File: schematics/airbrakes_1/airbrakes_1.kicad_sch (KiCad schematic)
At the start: 13 parts, among them U6 XL1509-3.3

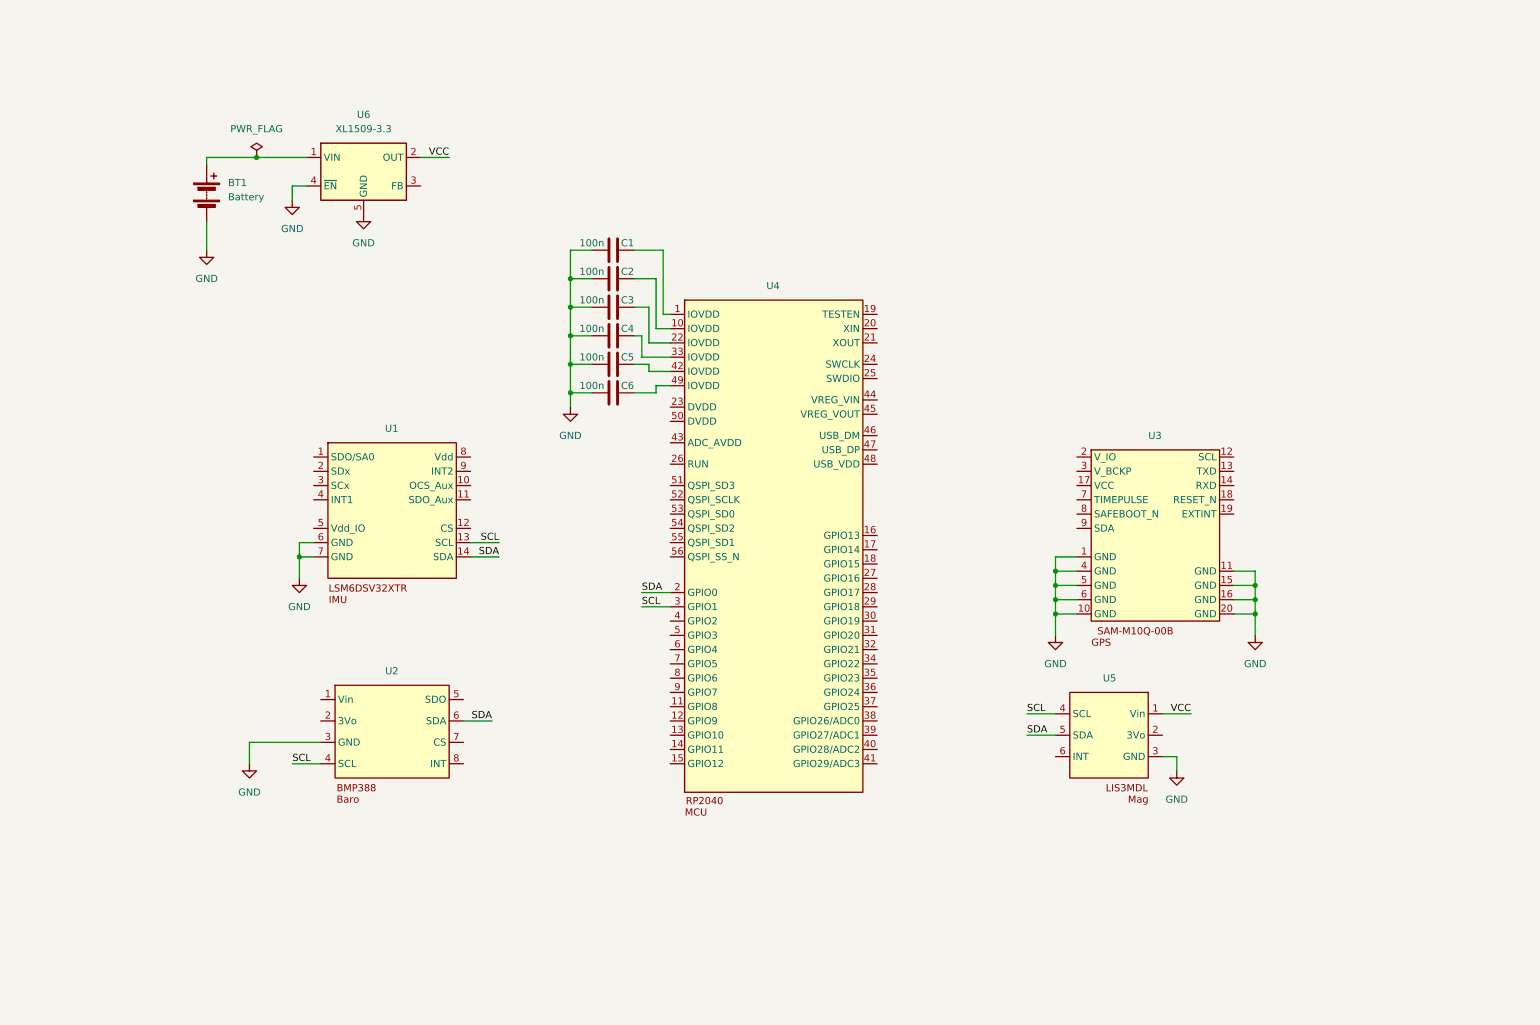
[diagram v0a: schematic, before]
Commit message: Route SPI/I2C connections to Baro, Mag, GPS; some other connections & notes
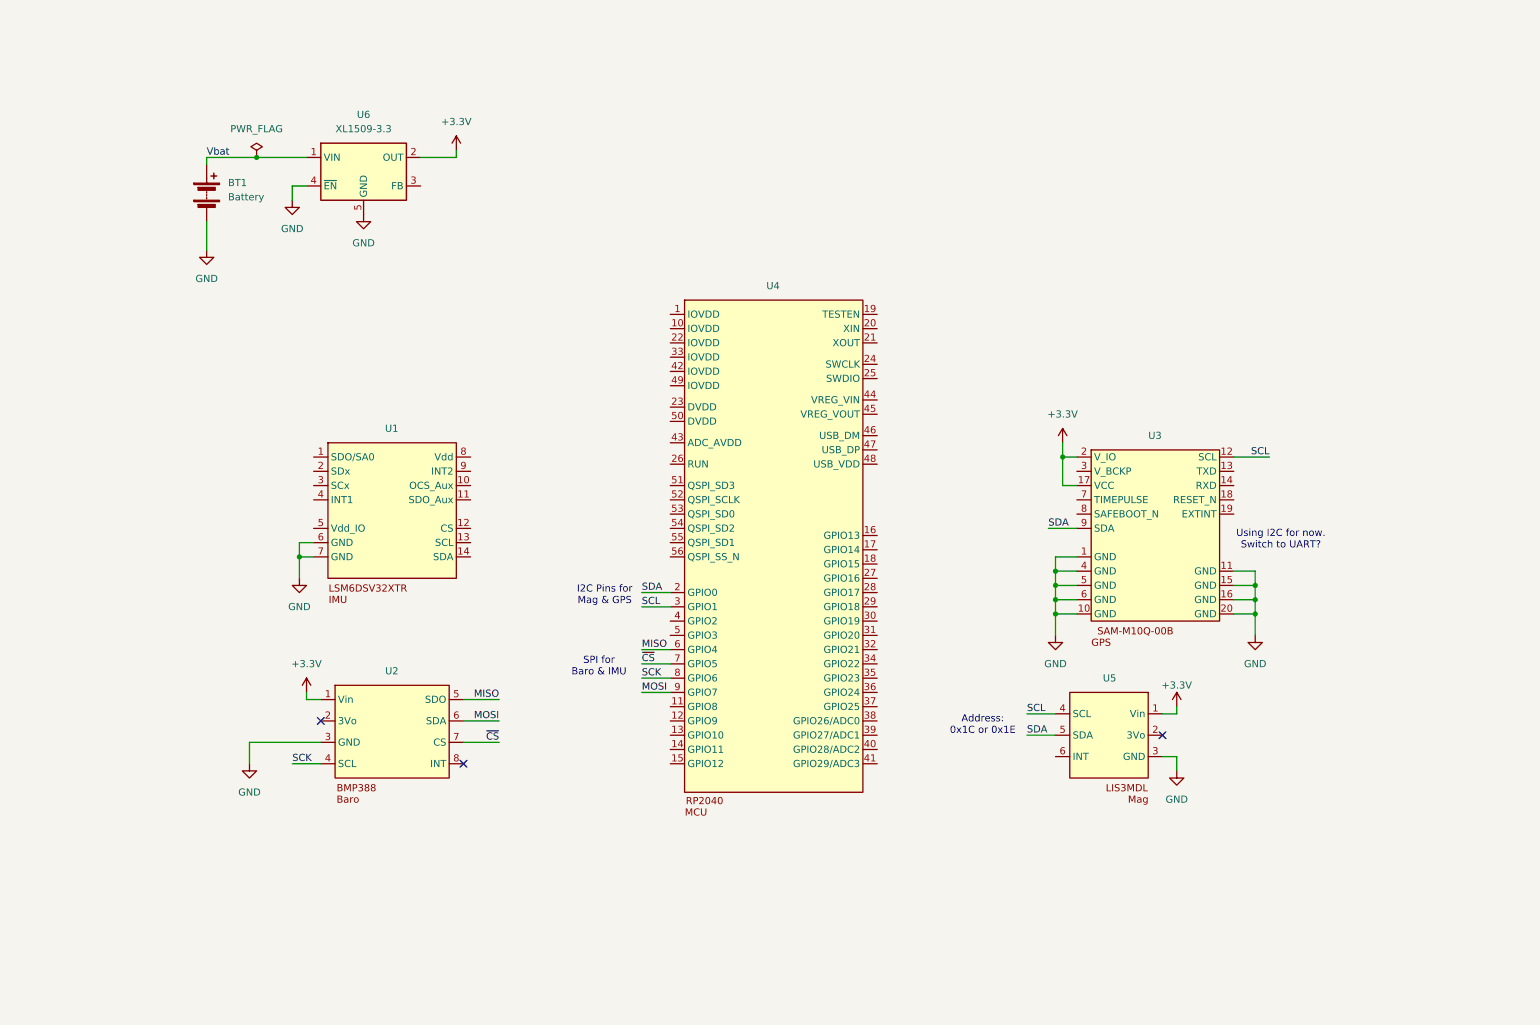
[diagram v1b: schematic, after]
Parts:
- removed C1, C2, C3, C4, C5, C6: 100n, symbol Device:C
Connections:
- net VCC is gone; now on net +3.3V: U5.1 (Vin), U6.2 (OUT)
- net SCL: now also U3.12 (SCL); no longer U1.13 (SCL), U2.4 (SCL)
- net SDA: now also U3.9 (SDA); no longer U1.14 (SDA), U2.6 (SDA)
- net +3.3V: now reaches U3.17 (VCC)
- net +3.3V: now also U2.1 (Vin), U3.2 (V_IO)
- net Vbat: now reaches BT1.1 (+), U6.1 (VIN)
- net MISO: now reaches U2.5 (SDO)
- net MISO: now also U4.6 (GPIO4)
- net ~{CS}: now reaches U2.7 (CS)
- net ~{CS}: now also U4.7 (GPIO5)
- net SCK: now reaches U4.8 (GPIO6)
- net SCK: now also U2.4 (SCL)
- net MOSI: now reaches U4.9 (GPIO7)
- net MOSI: now also U2.6 (SDA)
- no-connect marks 0 -> 3
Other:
- note added: "Address: 0x1C or 0x1E"
- note added: "I2C Pins for Mag & GPS"
- note added: "SPI for Baro & IMU"
- note added: "Using I2C for now. Switch to UART?"

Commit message: Finish communication routing, organize into sections
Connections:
- net +3.3V: now also U1.5 (Vdd_IO), U1.8 (Vdd)
- net GND: now also U1.2 (SDx), U1.3 (SCx)
- net MISO: now also U1.1 (SDO/SA0)
- net MOSI: now also U1.14 (SDA)
- net SCK: now also U1.13 (SCL)
- net ~{CS_imu}: now reaches U1.12 (CS)
- net ~{CS_imu}: now also U4.12 (GPIO9)
- net ~{CS} renamed ~{CS_baro}
- no-connect marks 3 -> 26
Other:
- note added: "Consider building out details, might use a premade board though"
- note added: "MCU"
- note added: "Power"
- note added: "Sensors"
- moved on the sheet: BT1, U1, U2, U3, U4, U5, U6

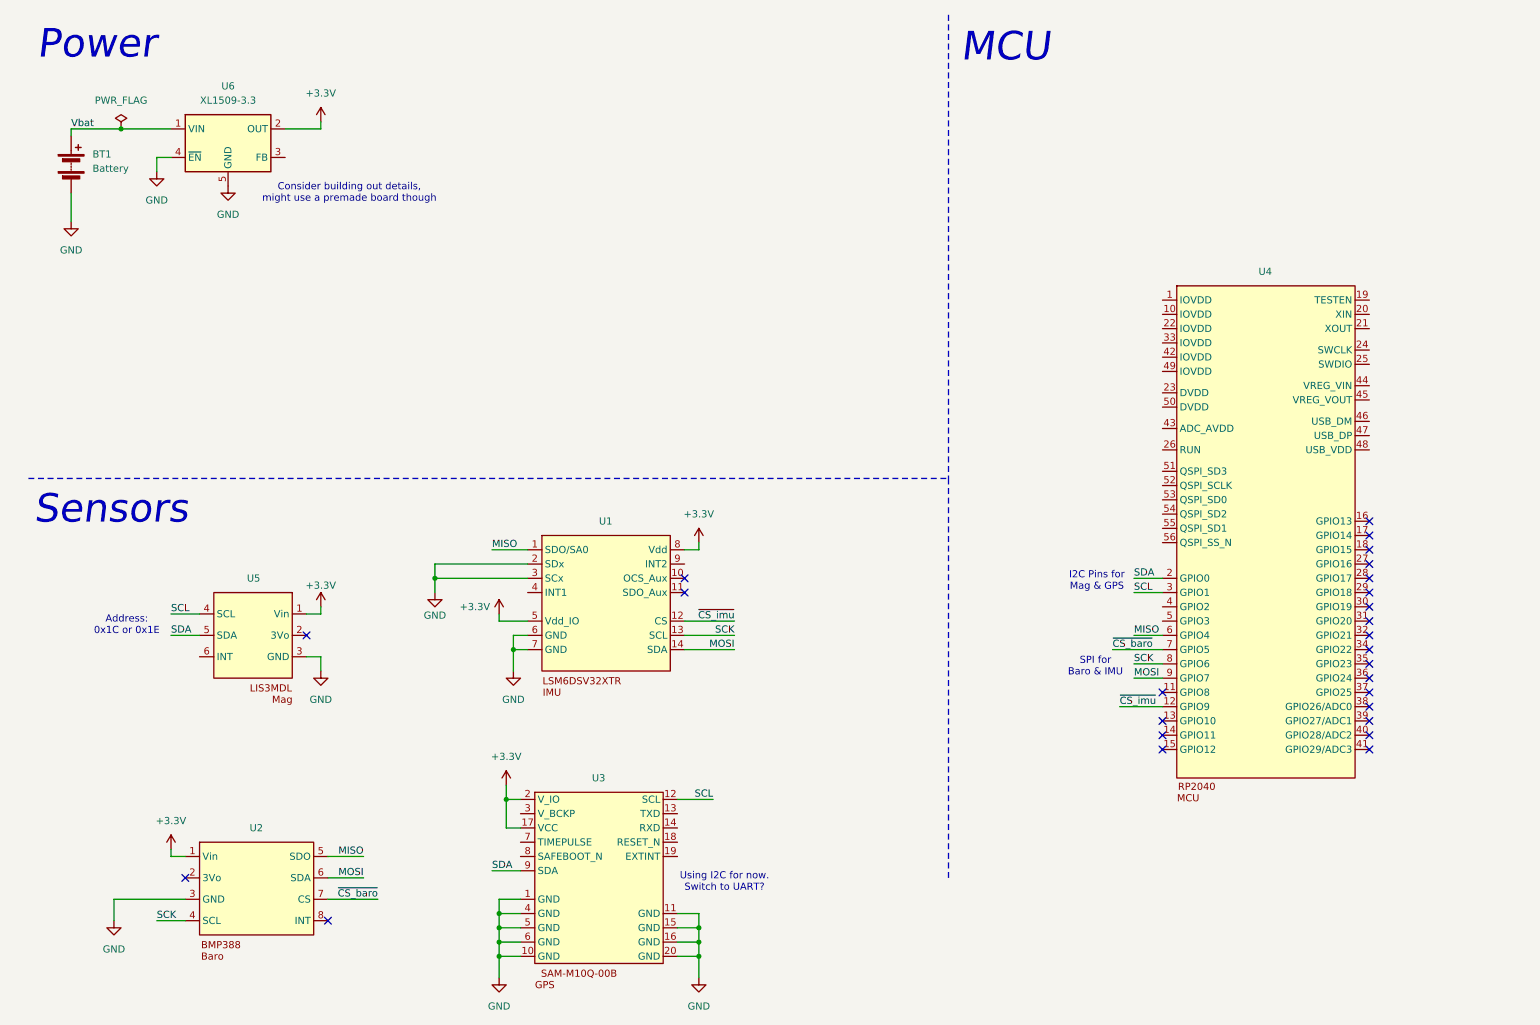
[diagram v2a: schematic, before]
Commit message: Add am-3637b motor
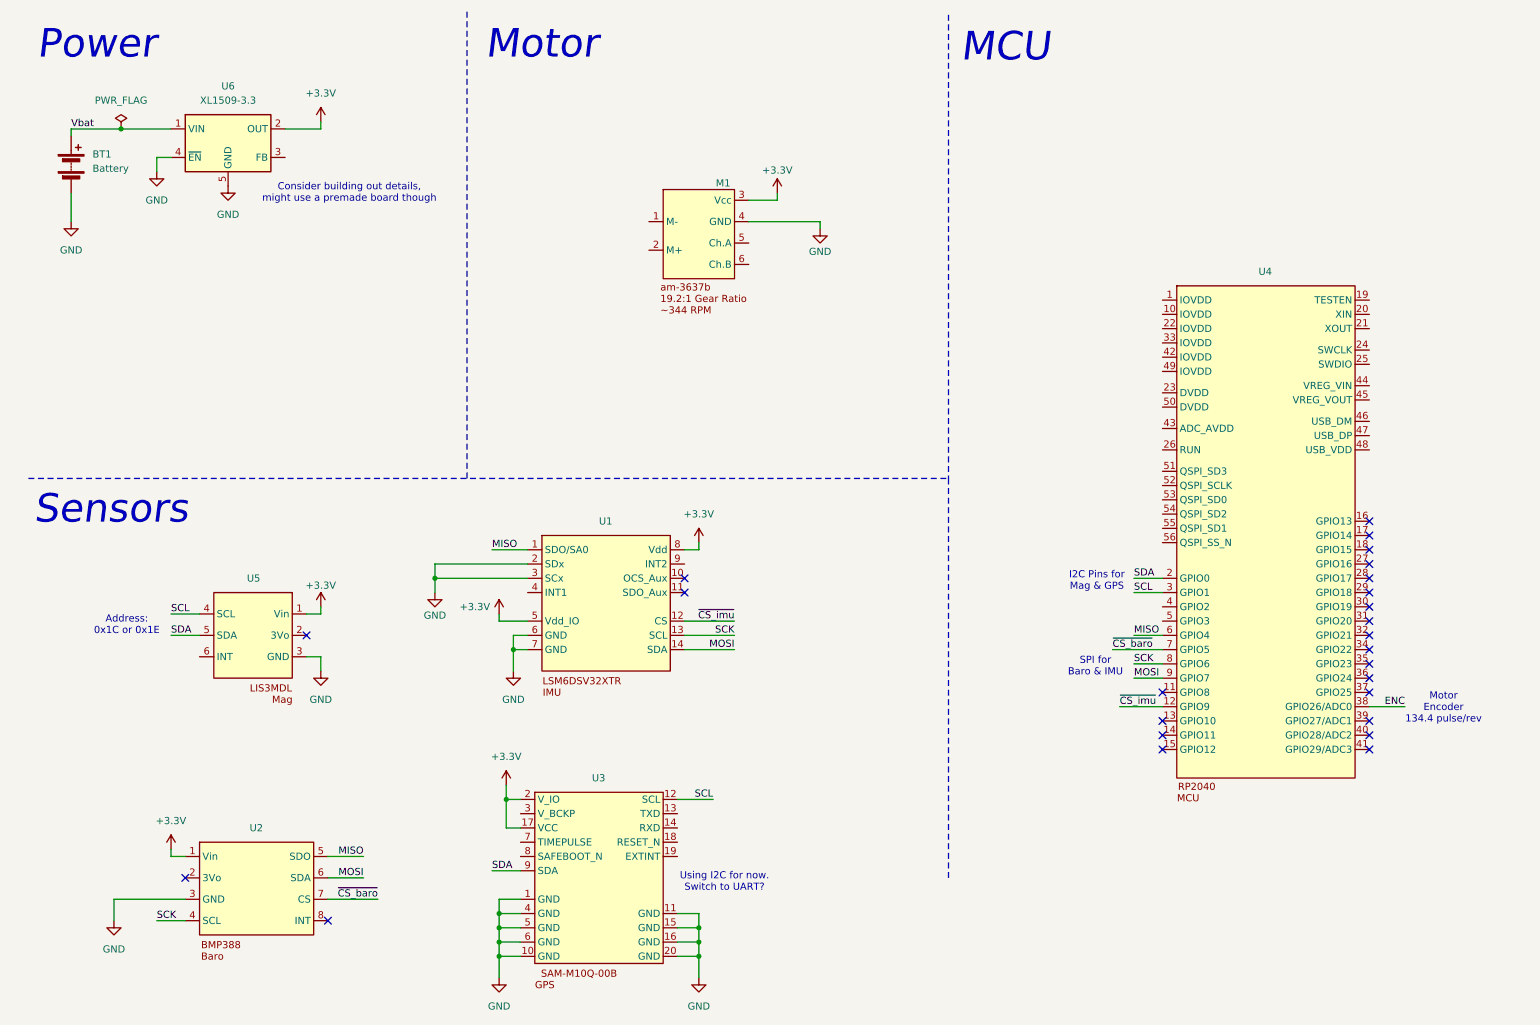
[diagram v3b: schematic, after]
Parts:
- added M1: (no value), symbol airbrakes_1:am-3637b
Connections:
- net +3.3V: now also M1.3 (Vcc)
- net GND: now also M1.4 (GND)
- net ENC: now reaches U4.38 (GPIO26/ADC0)
- no-connect marks 26 -> 25
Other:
- note added: "Motor"
- note added: "Motor Encoder 134.4 pulse/rev"

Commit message: Add SD Card peripheral
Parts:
- added J1: (no value), symbol airbrakes_1:Adafruit_4682
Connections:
- net +3.3V: now also U4.1 (IOVDD), U4.10 (IOVDD), U4.22 (IOVDD), U4.26 (RUN), U4.33 (IOVDD), U4.42 (IOVDD), U4.43 (ADC_AVDD), U4.44 (VREG_VIN), U4.49 (IOVDD), J1.1 (3V)
- net ENC: now also M1.5 (Ch.A)
- net GND: now also M1.1 (M-), J1.2 (GND)
- net MISO: now also J1.4 (SO)
- net MOSI: now also J1.5 (SI)
- net SCK: now also J1.3 (CLK)
- net +12V: now reaches M1.2 (M+)
- net ~{CS_SD}: now reaches U4.16 (GPIO13)
- net ~{CS_SD}: now also J1.6 (VSS)
- net +1V1: now reaches U4.23 (DVDD)
- net +1V1: now also U4.45 (VREG_VOUT), U4.50 (DVDD)
- new net SD_DET: J1.9 (DET)
- no-connect marks 25 -> 30
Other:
- note added: "Low when NO card inserted, pulled up via 4.7kΩ when inserted."
- note added: "Max efficiency @ 11.98V, 1.914A"
- note added: "Might want to use Ch.B? Test to see how outputs from these correspond to motor movement."
- note added: "SD Card"
- note added: "Uses SPI or SDIO"
- moved on the sheet: BT1, M1, U4, U6

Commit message: Create new project in schematics for teensy 4.1 mcu
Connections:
- net GND: now also U4.19 (TESTEN)
- net SCL: now also U4.16 (GPIO13); no longer U4.3 (GPIO1)
- net SDA: now also U4.15 (GPIO12); no longer U4.2 (GPIO0)
- net SD_DET: now also U4.39 (GPIO27/ADC1)
- net ~{CS_SD}: now also U4.3 (GPIO1); no longer U4.16 (GPIO13)
- no-connect marks 30 -> 28
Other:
- note added: "I2C CLK for Mag & GPS"
- note added: "I2C Data for Mag & GPS"
- note added: "Transferring data directly to SD Card from MCU. Transfer to flash memory first?"
- note removed: "I2C Pins for Mag & GPS"
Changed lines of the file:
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@@
 	(generator_version "10.0")
 	(paper "A4")
+	(text "Transferring data directly to\nSD Card from MCU.\nTransfer to flash memory first?"
+		(exclude_from_sim no)
+		(at 13.208 64.262 0)
+		(effects
+			(font
+				(size 1.27 1.27)
+			)
+			(justify left)
+		)
+	)
 	(text "SD Card"
 		(exclude_from_sim no)
@@
 	(text "Motor\nEncoder\n134.4 pulse/rev"
 		(exclude_from_sim no)
-		(at 264.668 119.634 0)
+		(at 266.954 114.554 0)
+		(effects
+			(font
+				(size 1.27 1.27)
+			)
+		)
+	)
+	(text "I2C Data for \nMag & GPS"
+		(exclude_from_sim no)
+		(at 202.692 127 0)
 		(effects
 			(font
@@
 		)
 	)
-	(text "I2C Pins for \nMag & GPS"
+	(text "I2C CLK for \nMag & GPS"
 		(exclude_from_sim no)
-		(at 202.946 97.028 0)
+		(at 263.398 86.36 0)
 		(effects
 			(font
@@
 	)
 	(no_connect
-		(at 251.46 121.92)
-	)
-	(no_connect
 		(at 251.46 99.06)
 	)
 	(no_connect
-		(at 214.63 127)
-	)
-	(no_connect
 		(at 251.46 116.84)
 	)
@@
 	(wire
 		(pts
-			(xy 209.55 99.06) (xy 214.63 99.06)
+			(xy 256.54 86.36) (xy 251.46 86.36)
 		)
 		(stroke
@@
 	(wire
 		(pts
-			(xy 251.46 86.36) (xy 259.08 86.36)
+			(xy 214.63 99.06) (xy 207.01 99.06)
 		)
 		(stroke
@@
 	(wire
 		(pts
+			(xy 251.46 46.99) (xy 264.16 46.99)
+		)
+		(stroke
+			(width 0)
+			(type default)
+		)
+	)
+	(wire
+		(pts
 			(xy 31.75 27.94) (xy 40.64 27.94)
 		)
@@
 	(wire
 		(pts
+			(xy 264.16 46.99) (xy 264.16 48.26)
+		)
+		(stroke
+			(width 0)
+			(type default)
+		)
+	)
+	(wire
+		(pts
 			(xy 40.64 162.56) (xy 38.1 162.56)
 		)
@@
 	(wire
 		(pts
+			(xy 251.46 121.92) (xy 260.35 121.92)
+		)
+		(stroke
+			(width 0)
+			(type default)
+		)
+	)
+	(wire
+		(pts
 			(xy 208.28 57.15) (xy 208.28 59.69)
 		)
@@
 	(wire
 		(pts
-			(xy 209.55 96.52) (xy 214.63 96.52)
+			(xy 209.55 127) (xy 214.63 127)
 		)
 		(stroke
@@
 	)
 	(label "SDA"
-		(at 209.55 96.52 0)
+		(at 209.55 127 0)
 		(effects
 			(font
@@
 	)
 	(label "SCL"
-		(at 209.55 99.06 0)
+		(at 256.54 86.36 180)
 		(effects
 			(font
 				(size 1.27 1.27)
 			)
-			(justify left bottom)
+			(justify right bottom)
 		)
 	)
@@
 	)
 	(label "~{CS_SD}"
-		(at 259.08 86.36 180)
+		(at 207.01 99.06 0)
 		(effects
 			(font
 				(size 1.27 1.27)
 			)
-			(justify right bottom)
+			(justify left bottom)
 		)
 	)
@@
 		)
 	)
+	(label "SD_DET"
+		(at 260.35 121.92 180)
+		(effects
+			(font
+				(size 1.27 1.27)
+			)
+			(justify right bottom)
+		)
+	)
 	(label "SCK"
 		(at 44.45 62.23 0)
@@
 		(in_pos_files yes)
 		(dnp no)
-		(fields_autoplaced yes)
 		(property "Reference" "#PWR021"
 			(at 270.51 62.23 0)
@@
 		)
 		(property "Value" "+3.3V"
-			(at 270.51 53.34 0)
+			(at 270.51 54.61 0)
 			(show_name no)
 			(do_not_autoplace no)
@@
 		(in_pos_files yes)
 		(dnp no)
-		(fields_autoplaced yes)
 		(property "Reference" "#PWR022"
 			(at 276.86 62.23 0)
@@
 		)
 		(property "Value" "+1V1"
-			(at 276.86 53.34 0)
+			(at 276.86 54.61 0)
 			(show_name no)
 			(do_not_autoplace no)
@@
 					(unit 1)
 				)
+			)
+		)
+	)
+	(symbol
+		(lib_id "power:GND")
+		(at 264.16 48.26 0)
+		(unit 1)
+		(body_style 1)
+		(exclude_from_sim no)
+		(in_bom yes)
+		(on_board yes)
+		(in_pos_files yes)
+		(dnp no)
+		(property "Reference" "#PWR027"
+			(at 264.16 54.61 0)
+			(hide yes)
+			(show_name no)
+			(do_not_autoplace no)
+			(effects
+				(font
+					(size 1.27 1.27)
+				)
+			)
+		)
+		(property "Value" "GND"
+			(at 267.716 50.038 0)
+			(show_name no)
+			(do_not_autoplace no)
+			(effects
+				(font
+					(size 1.27 1.27)
+				)
+			)
+		)
+		(property "Footprint" ""
+			(at 264.16 48.26 0)
+			(hide yes)
+			(show_name no)
+			(do_not_autoplace no)
+			(effects
+				(font
+					(size 1.27 1.27)
+				)
+			)
+		)
+		(property "Datasheet" ""
+			(at 264.16 48.26 0)
+			(hide yes)
+			(show_name no)
+			(do_not_autoplace no)
+			(effects
+				(font
+					(size 1.27 1.27)
+				)
+			)
+		)
+		(property "Description" "Power symbol creates a global label with name \"GND\" , ground"
+			(at 264.16 48.26 0)
+			(hide yes)
+			(show_name no)
+			(do_not_autoplace no)
+			(effects
+				(font
+					(size 1.27 1.27)
+				)
+			)
+		)
+		(pin "1"
+		)
+		(instances
+			(project "airbrakes_1"
+				(path "/4056183e-e49a-49da-b487-53d090193030"
+					(reference "#PWR027")
+					(unit 1)
+				)
